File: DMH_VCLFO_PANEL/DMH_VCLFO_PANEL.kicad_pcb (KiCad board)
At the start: 2 copper layers, 100 x 200 mm, 47 parts, among them J0 Panel_GND_Solder_Wire_Pad

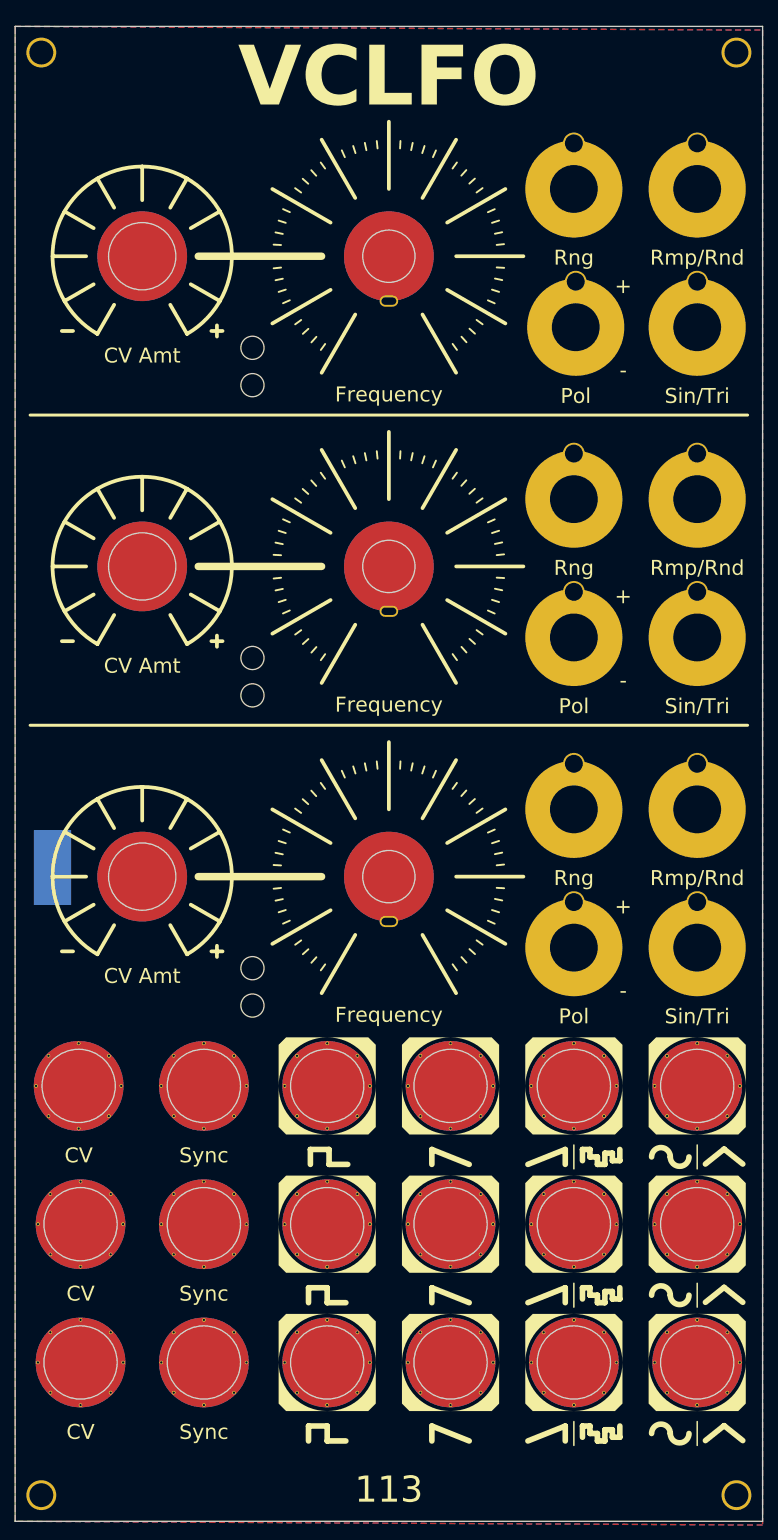
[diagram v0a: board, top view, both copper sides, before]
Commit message: Modified front panel
Added V/Oct calib trimpot hole
Replaced Polarity switch with Bus CV
Added Fine as normalized function of CV Amt pot
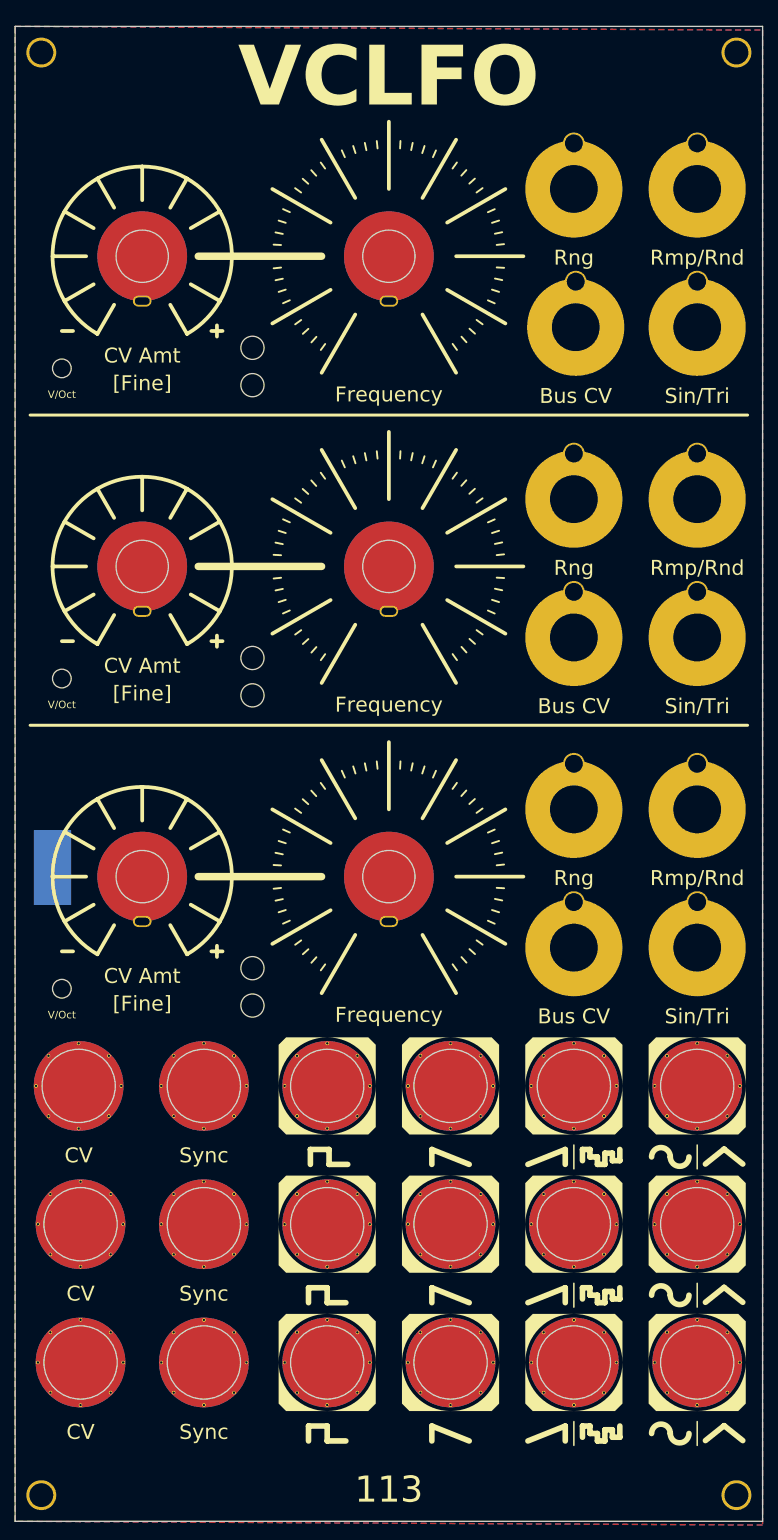
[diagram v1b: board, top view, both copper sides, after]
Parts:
- added H47: V/Oct, SynthStuff:MountingHole_TrimPot, F.Cu at (56.2, 75.8)
- added H48: V/Oct, SynthStuff:MountingHole_TrimPot, F.Cu at (56.2, 117.2)
- added H49: V/Oct, SynthStuff:MountingHole_TrimPot, F.Cu at (56.2, 158.8)
- H13, H18, H28: footprint SynthStuff:Pot_Cutout_Tiny_attv_P110KH1 -> SynthStuff:Pot_Cutout_Tiny_attv_RD901F
- H44, H45, H46: value Pol -> Bus CV
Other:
- board text added: "[Fine]"
- board text removed: "+"
- board text removed: "-"

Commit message: Sch redesign in progress
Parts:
- added H50: Fine Rng, SynthStuff:MountingHole_TrimPot, F.Cu at (56.2, 44.8)
- added H51: Fine Rng, SynthStuff:MountingHole_TrimPot, F.Cu at (56.2, 86.2)
- added H52: Fine Rng, SynthStuff:MountingHole_TrimPot, F.Cu at (56.2, 127.8)

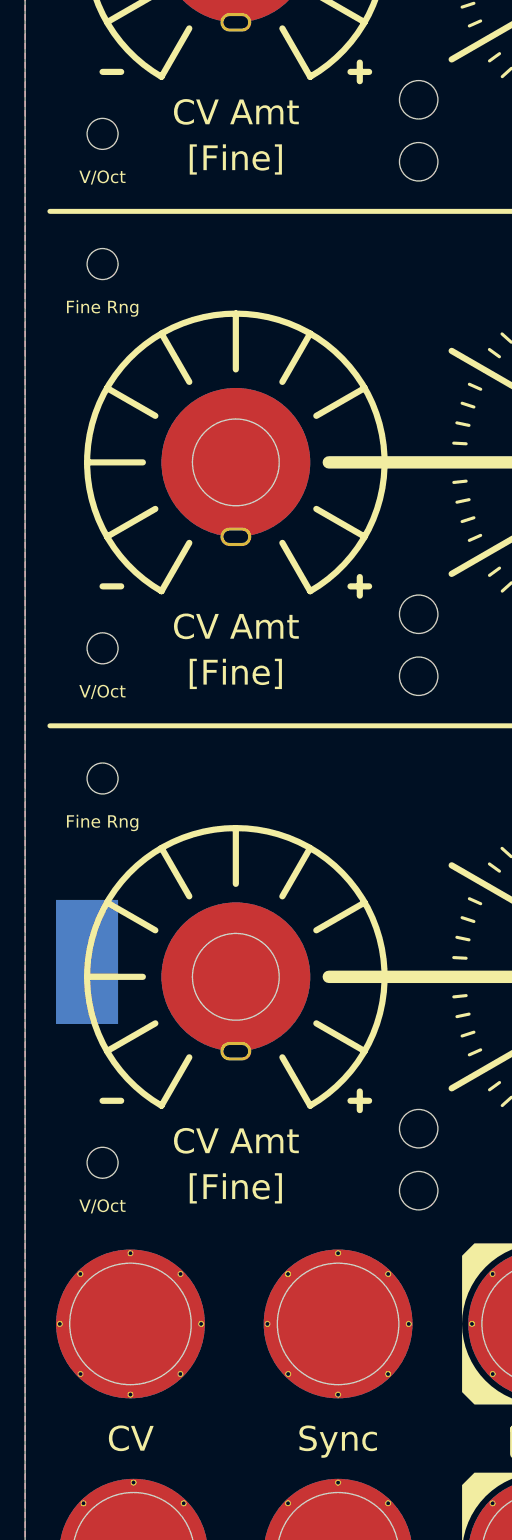
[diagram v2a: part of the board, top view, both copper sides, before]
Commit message: Controls PCB comp placement in progress
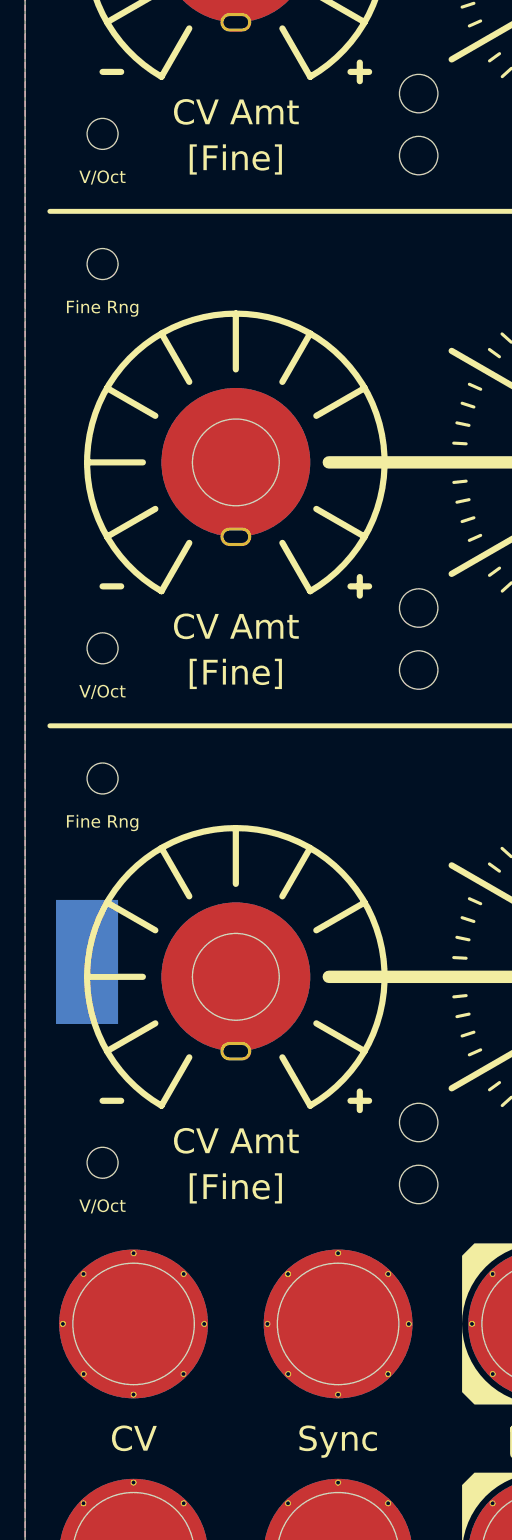
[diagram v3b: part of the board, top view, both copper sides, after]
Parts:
- moved H14 0.50 mm to (81.8, 72.5)
- moved H15 0.50 mm to (81.8, 114.0)
- moved H25 0.50 mm to (81.8, 155.5)
- moved H36 0.50 mm to (81.8, 77.5)
- moved H37 0.50 mm to (81.8, 119.0)
- moved H38 0.50 mm to (81.8, 160.5)
- moved H5 0.25 mm to (58.8, 171.8)
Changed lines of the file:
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@@
 	(footprint "SynthStuff:MountingHole_LED_3mm_Y"
 		(layer "F.Cu")
-		(at 81.75 78)
+		(at 81.75 77.5)
 		(descr "Mounting Hole 3mm, no annular")
 		(tags "mounting hole 3mm no annular")
@@
 	(footprint "SynthStuff:MountingHole_LED_3mm_Y"
 		(layer "F.Cu")
-		(at 81.75 161)
+		(at 81.75 160.5)
 		(descr "Mounting Hole 3mm, no annular")
 		(tags "mounting hole 3mm no annular")
@@
 	(footprint "SynthStuff:MountingHole_LED_3mm_Y"
 		(layer "F.Cu")
-		(at 81.75 119.5)
+		(at 81.75 119)
 		(descr "Mounting Hole 3mm, no annular")
 		(tags "mounting hole 3mm no annular")
@@
 	(footprint "SynthStuff:MountingHole_LED_3mm_R"
 		(layer "F.Cu")
-		(at 81.75 156)
+		(at 81.75 155.5)
 		(descr "Mounting Hole 3mm, no annular")
 		(tags "mounting hole 3mm no annular")
@@
 	(footprint "SynthStuff:MountingHole_LED_3mm_R"
 		(layer "F.Cu")
-		(at 81.75 73)
+		(at 81.75 72.5)
 		(descr "Mounting Hole 3mm, no annular")
 		(tags "mounting hole 3mm no annular")
@@
 	(footprint "SynthStuff:MountingHole_LED_3mm_R"
 		(layer "F.Cu")
-		(at 81.75 114.5)
+		(at 81.75 114)
 		(descr "Mounting Hole 3mm, no annular")
 		(tags "mounting hole 3mm no annular")
@@
 	(footprint "SynthStuff:Jack_6.35mm_Cutout_v3"
 		(layer "F.Cu")
-		(at 58.5 171.75)
+		(at 58.75 171.75)
 		(property "Reference" "H5"
 			(at 0 -6 0)
@@
 				(polygon
 					(pts
-						(xy 58.184072 181.381622) (xy 57.192934 181.381622) (xy 57.114867 181.377793) (xy 57.044608 181.366621)
-						(xy 56.983505 181.34921) (xy 56.928978 181.325764) (xy 56.8381 181.262471) (xy 56.81216 181.236297)
-						(xy 56.775385 181.191015) (xy 56.744745 181.140905) (xy 56.720936 181.086916) (xy 56.704405 181.029528)
-						(xy 56.694557 180.9371) (xy 56.709583 180.82238) (xy 56.754084 180.714483) (xy 56.78672 180.66557)
-						(xy 56.825412 180.621628) (xy 56.834508 180.612868) (xy 56.882716 180.573763) (xy 56.937672 180.541226)
-						(xy 56.992445 180.518752) (xy 57.054556 180.502381) (xy 57.192934 180.489891) (xy 58.184072 180.489891)
-						(xy 58.184072 179.988583) (xy 57.192934 179.988583) (xy 57.089055 179.992432) (xy 56.991419 180.003747)
-						(xy 56.900714 180.021962) (xy 56.815763 180.046811) (xy 56.736096 180.078084) (xy 56.661856 180.115355)
-						(xy 56.526325 180.208664) (xy 56.492934 180.237833) (xy 56.377396 180.366029) (xy 56.328674 180.437571)
-						(xy 56.286487 180.513541) (xy 56.251601 180.592581) (xy 56.223893 180.675118) (xy 56.204071 180.759061)
-						(xy 56.1919 180.845581) (xy 56.187753 180.934413) (xy 56.202933 181.106905) (xy 56.247793 181.27126)
-						(xy 56.320971 181.423674) (xy 56.420298 181.559677) (xy 56.431385 181.572009) (xy 56.492162 181.632846)
-						(xy 56.558681 181.687887) (xy 56.628203 181.735027) (xy 56.703247 181.776135) (xy 56.782026 181.81017)
-						(xy 56.866272 181.837823) (xy 56.955361 181.858653) (xy 57.050018 181.872602) (xy 57.192934 181.88)
-						(xy 58.184072 181.88)
+						(xy 58.434072 181.381622) (xy 57.442934 181.381622) (xy 57.364867 181.377793) (xy 57.294608 181.366621)
+						(xy 57.233505 181.34921) (xy 57.178978 181.325764) (xy 57.0881 181.262471) (xy 57.06216 181.236297)
+						(xy 57.025385 181.191015) (xy 56.994745 181.140905) (xy 56.970936 181.086916) (xy 56.954405 181.029528)
+						(xy 56.944557 180.9371) (xy 56.959583 180.82238) (xy 57.004084 180.714483) (xy 57.03672 180.66557)
+						(xy 57.075412 180.621628) (xy 57.084508 180.612868) (xy 57.132716 180.573763) (xy 57.187672 180.541226)
+						(xy 57.242445 180.518752) (xy 57.304556 180.502381) (xy 57.442934 180.489891) (xy 58.434072 180.489891)
+						(xy 58.434072 179.988583) (xy 57.442934 179.988583) (xy 57.339055 179.992432) (xy 57.241419 180.003747)
+						(xy 57.150714 180.021962) (xy 57.065763 180.046811) (xy 56.986096 180.078084) (xy 56.911856 180.115355)
+						(xy 56.776325 180.208664) (xy 56.742934 180.237833) (xy 56.627396 180.366029) (xy 56.578674 180.437571)
+						(xy 56.536487 180.513541) (xy 56.501601 180.592581) (xy 56.473893 180.675118) (xy 56.454071 180.759061)
+						(xy 56.4419 180.845581) (xy 56.437753 180.934413) (xy 56.452933 181.106905) (xy 56.497793 181.27126)
+						(xy 56.570971 181.423674) (xy 56.670298 181.559677) (xy 56.681385 181.572009) (xy 56.742162 181.632846)
+						(xy 56.808681 181.687887) (xy 56.878203 181.735027) (xy 56.953247 181.776135) (xy 57.032026 181.81017)
+						(xy 57.116272 181.837823) (xy 57.205361 181.858653) (xy 57.300018 181.872602) (xy 57.442934 181.88)
+						(xy 58.434072 181.88)
 					)
 				)
 				(polygon
 					(pts
-						(xy 59.049302 181.572254) (xy 59.085748 181.643246) (xy 59.127114 181.705918) (xy 59.170235 181.756923)
-						(xy 59.217875 181.800835) (xy 59.268286 181.836575) (xy 59.323126 181.865819) (xy 59.447189 181.905194)
-						(xy 59.598116 181.919078) (xy 59.681748 181.915156) (xy 59.758784 181.903334) (xy 59.824383 181.885292)
-						(xy 59.884757 181.860352) (xy 59.938027 181.829831) (xy 59.986837 181.792821) (xy 60.072096 181.698673)
-						(xy 60.143999 181.572254) (xy 60.82165 180.072602) (xy 60.852425 179.988583) (xy 60.261601 179.988583)
-						(xy 60.239253 180.05575) (xy 59.679204 181.362327) (xy 59.661896 181.392458) (xy 59.641721 181.410856)
-						(xy 59.600802 181.421067) (xy 59.57359 181.416974) (xy 59.549154 181.40395) (xy 59.519714 181.362327)
-						(xy 58.954047 180.05575) (xy 58.934508 179.988583) (xy 58.335258 179.988583) (xy 58.366033 180.072602)
+						(xy 59.299302 181.572254) (xy 59.335748 181.643246) (xy 59.377114 181.705918) (xy 59.420235 181.756923)
+						(xy 59.467875 181.800835) (xy 59.518286 181.836575) (xy 59.573126 181.865819) (xy 59.697189 181.905194)
+						(xy 59.848116 181.919078) (xy 59.931748 181.915156) (xy 60.008784 181.903334) (xy 60.074383 181.885292)
+						(xy 60.134757 181.860352) (xy 60.188027 181.829831) (xy 60.236837 181.792821) (xy 60.322096 181.698673)
+						(xy 60.393999 181.572254) (xy 61.07165 180.072602) (xy 61.102425 179.988583) (xy 60.511601 179.988583)
+						(xy 60.489253 180.05575) (xy 59.929204 181.362327) (xy 59.911896 181.392458) (xy 59.891721 181.410856)
+						(xy 59.850802 181.421067) (xy 59.82359 181.416974) (xy 59.799154 181.40395) (xy 59.769714 181.362327)
+						(xy 59.204047 180.05575) (xy 59.184508 179.988583) (xy 58.585258 179.988583) (xy 58.616033 180.072602)
 					)
 				)

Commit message: Generated Gerbers
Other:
- board text added: "558"
- board text added: "Mk1.0 - March 2026"
- board text removed: "113"
- board text removed: "Mk1.0 - Month Year"
